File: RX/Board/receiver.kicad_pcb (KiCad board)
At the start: 2 copper layers, 31.8 x 76.2 mm, 16 parts, among them J1 CONN_SWITCH, J2 PROG_CONN, J3 RX_JMP, J4 TX_JMP, J5 AT_MODE_JUMP, J6 BATT_CONN, J7 GENERIC, U1 ARDUINO_PRO_MINI, U2 ITEAD_HC-05

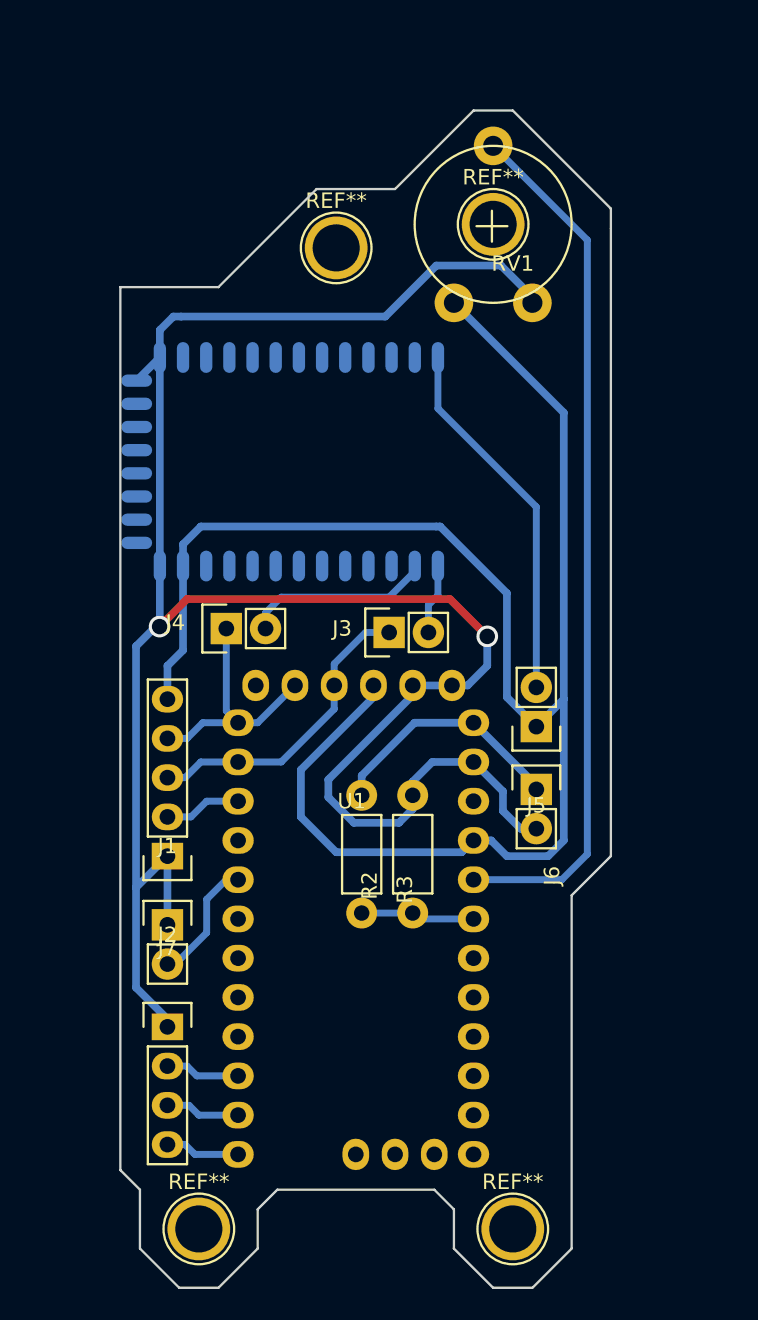
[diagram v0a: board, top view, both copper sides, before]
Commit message: Corrected bugs and added first prototype of receiver board
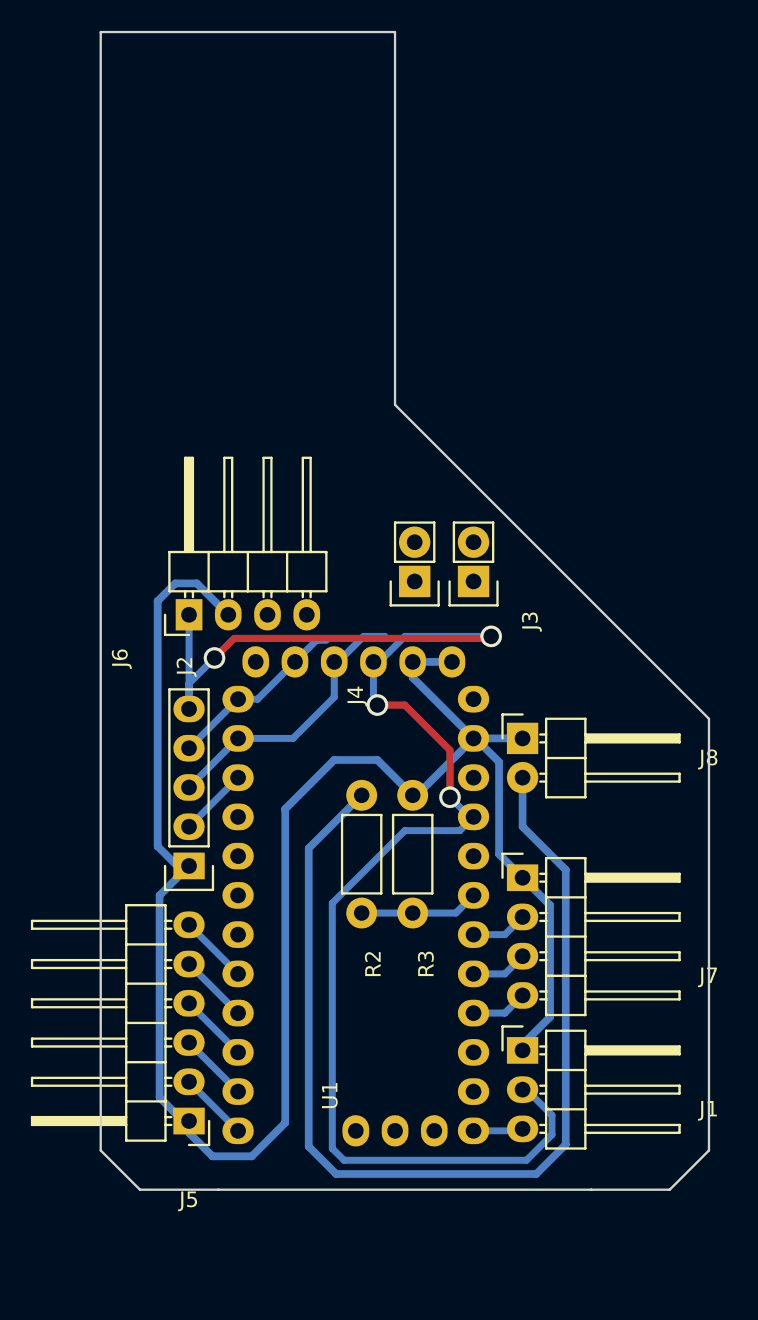
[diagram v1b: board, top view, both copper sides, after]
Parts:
- removed REF** (x4): 1pin, Connect:1pin
- removed RV1: POT, foots:Potenziometro_PIHER_10mm_diametro
- removed U2: ITEAD_HC-05, foots:HC-05
- added J8: BIG_BATTERY, Pin_Headers:Pin_Header_Angled_1x02, F.Cu at (169.5, 124.0)
- J1: value CONN_SWITCH -> ESC; footprint Pin_Headers:Pin_Header_Straight_1x02 -> Pin_Headers:Pin_Header_Angled_1x03
- J5: value AT_MODE_JUMP -> LIGHTS; footprint Pin_Headers:Pin_Header_Straight_1x02 -> Pin_Headers:Pin_Header_Angled_1x06
- J6: value BATT_CONN -> Bluetooth; footprint Pin_Headers:Pin_Header_Straight_1x02 -> Pin_Headers:Pin_Header_Angled_1x04
- J7: footprint Pin_Headers:Pin_Header_Straight_1x04 -> Pin_Headers:Pin_Header_Angled_1x04
- moved J5 34.0 mm to (148.0, 148.7)
- moved J6 25.2 mm to (148.0, 116.0), turned to 90 degrees
- moved J7 24.9 mm to (169.5, 133.0)
- moved J1 24.4 mm to (169.5, 144.1)
- moved J4 12.6 mm to (162.6, 113.8), turned to 180 degrees
- moved J3 6.38 mm to (166.4, 113.8), turned to 180 degrees
- moved J2 1.53 mm to (148.0, 132.2)
- moved U1 1.52 mm to (158.8, 118.9)
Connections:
- J1 pad 2: SWITCH_PRESENZA -> +5V
- J2 pad 5: +3V3 -> +5V
- J5 pad 1: +3V3 -> GNDREF
- J5 pad 2: AT_MODE -> LIGHT_1
- J6 pad 1: +BATT -> +5V
- U1 pad 10: G3 -> LIGHT_3
- U1 pad 11: G2 -> LIGHT_2
- U1 pad 12: G1 -> LIGHT_1
- U1 pad 16: (no net) -> ESC_SIG
- U1 pad 19: (no net) -> G1
- U1 pad 20: (no net) -> G2
- U1 pad 21: (no net) -> G3
- U1 pad 23: ACCEL_POT -> (no net)
- U1 pad 24: +3V3 -> +5V
- U1 pad 27: +BATT -> (no net)
- U1 pad 30: +3V3 -> +5V
- U1 pad 5: SWITCH_PRESENZA -> (no net)
- U1 pad 8: (no net) -> LIGHT_5
- U1 pad 9: (no net) -> LIGHT_4
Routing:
- net +3V3: track 112.9 -> 0.00 mm
- net +5V: track 0.00 -> 97.2 mm, vias 0 -> 4
- net ACCEL_POT: track 56.4 -> 0.00 mm
- net +BATT: track 15.9 -> 67.2 mm
- net AT_MODE: track 24.0 -> 0.00 mm
- net GNDREF: track 142.3 -> 122.8 mm, vias 2 -> 0
- net RX_BT: track 12.1 -> 0.00 mm
- net SWITCH_PRESENZA: track 8.10 -> 0.00 mm
- net TX_BT: track 4.55 -> 0.00 mm
- net LIGHT_5: track 0.00 -> 4.49 mm
- net LIGHT_4: track 0.00 -> 4.49 mm
- net LIGHT_2: track 0.00 -> 4.49 mm
- net LIGHT_1: track 0.00 -> 4.49 mm
- net LIGHT_3: track 0.00 -> 4.49 mm
- net TX_ARD: track 16.1 -> 11.8 mm
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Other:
- board size 31.8 x 76.2 mm -> 39.4 x 74.9 mm

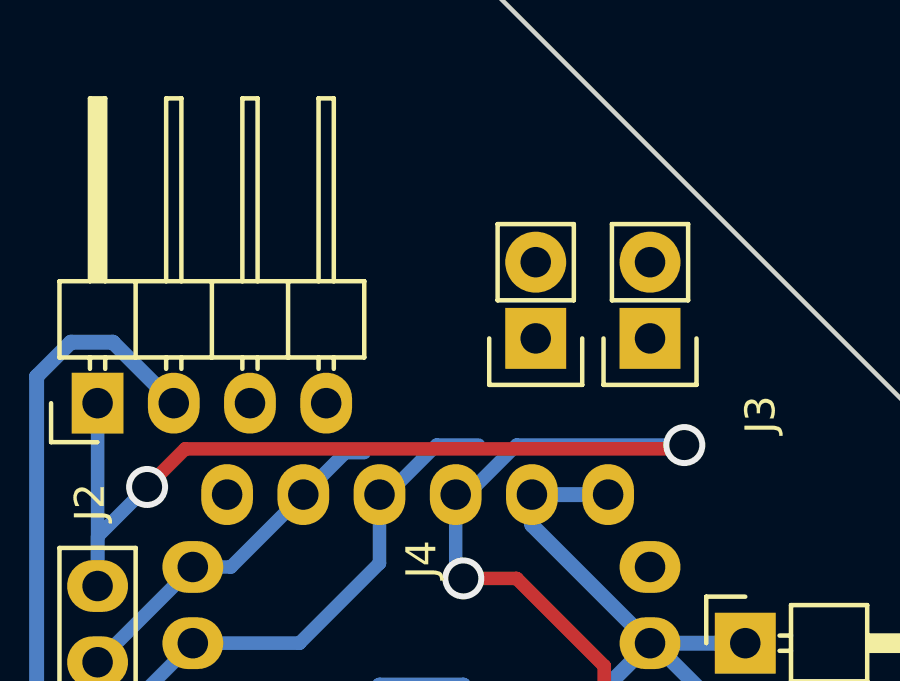
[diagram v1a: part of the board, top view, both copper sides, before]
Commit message: First working version of the receiver board
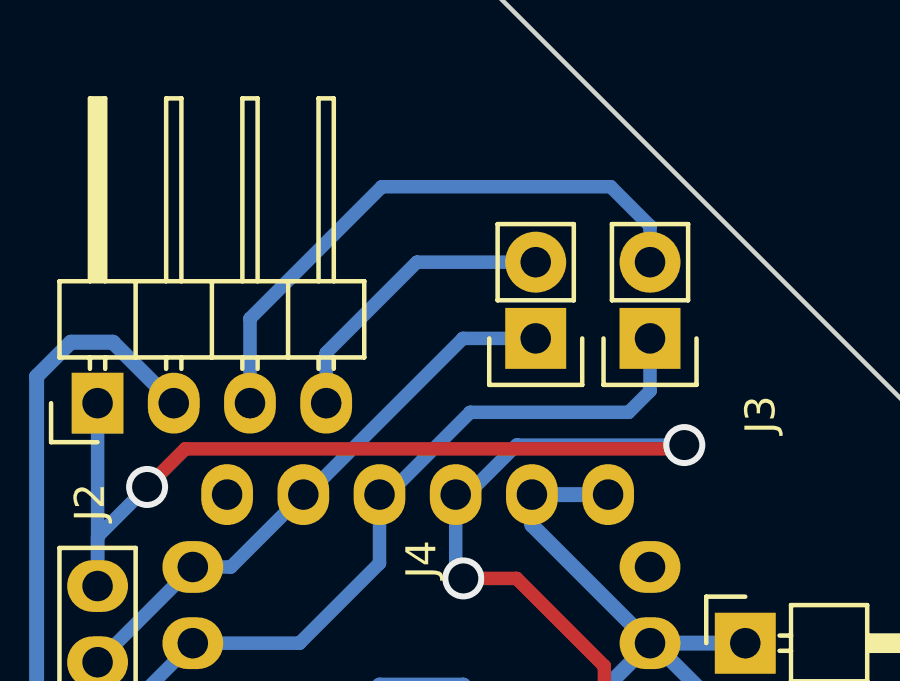
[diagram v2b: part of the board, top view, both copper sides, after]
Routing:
- net TX_BT: track 0.00 -> 19.7 mm
- net RX_BT: track 0.00 -> 9.91 mm
- net RX_ARD: track 18.1 -> 26.3 mm
- net TX_ARD: track 11.8 -> 19.1 mm
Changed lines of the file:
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@@
   (general
     (links 34)
-    (no_connects 4)
+    (no_connects 0)
     (area 137.079999 78.156999 189.675477 154.892)
     (thickness 1.6)
     (drawings 14)
-    (tracks 99)
+    (tracks 110)
     (zones 0)
     (modules 11)
@@
     (visible_elements FFFFFF7F)
     (pcbplotparams
-      (layerselection 0x01000_00000000)
+      (layerselection 0x00000_80000000)
       (usegerberextensions false)
       (excludeedgelayer true)
@@
   (segment (start 146.05 147.193) (end 146.05 134.112) (width 0.5) (layer B.Cu) (net 1))
   (segment (start 146.05 134.112) (end 147.955 132.207) (width 0.5) (layer B.Cu) (net 1) (status 20))
-  (segment (start 154.813 118.999) (end 156.21 117.602) (width 0.45) (layer B.Cu) (net 2) (status 10))
-  (segment (start 156.21 117.602) (end 156.845 117.602) (width 0.45) (layer B.Cu) (net 2))
+  (segment (start 154.813 118.999) (end 154.9273 118.999) (width 0.45) (layer B.Cu) (net 2) (status C00000))
+  (segment (start 154.9273 118.999) (end 160.1343 113.792) (width 0.45) (layer B.Cu) (net 2) (status 400000))
+  (segment (start 160.1343 113.792) (end 162.56 113.792) (width 0.45) (layer B.Cu) (net 2) (status 800000))
   (segment (start 151.13 121.412) (end 152.4 121.412) (width 0.45) (layer B.Cu) (net 2) (status 10))
   (segment (start 152.4 121.412) (end 154.813 118.999) (width 0.45) (layer B.Cu) (net 2) (status 20))
   (segment (start 147.955 124.587) (end 151.13 121.412) (width 0.45) (layer B.Cu) (net 2) (status 30))
-  (segment (start 157.353 118.999) (end 157.607 118.999) (width 0.45) (layer B.Cu) (net 3) (status 30))
-  (segment (start 157.607 118.999) (end 159.258 117.348) (width 0.45) (layer B.Cu) (net 3) (status 10))
-  (segment (start 159.258 117.348) (end 160.655 117.348) (width 0.45) (layer B.Cu) (net 3))
+  (segment (start 157.353 118.999) (end 157.6324 118.999) (width 0.45) (layer B.Cu) (net 3) (status C00000))
+  (segment (start 157.6324 118.999) (end 160.3756 116.2558) (width 0.45) (layer B.Cu) (net 3) (status 400000))
+  (segment (start 166.37 115.5446) (end 166.37 113.792) (width 0.45) (layer B.Cu) (net 3) (status 800000))
+  (segment (start 165.6588 116.2558) (end 166.37 115.5446) (width 0.45) (layer B.Cu) (net 3))
+  (segment (start 160.3756 116.2558) (end 165.6588 116.2558) (width 0.45) (layer B.Cu) (net 3))
   (segment (start 157.353 118.999) (end 157.353 121.285) (width 0.45) (layer B.Cu) (net 3) (status 10))
   (segment (start 154.686 123.952) (end 157.353 121.285) (width 0.45) (layer B.Cu) (net 3))
@@
   (segment (start 159.131 135.255) (end 162.433 135.255) (width 0.45) (layer B.Cu) (net 5) (status 30))
   (segment (start 147.955 129.667) (end 151.13 126.492) (width 0.45) (layer B.Cu) (net 6) (status 30))
+  (segment (start 166.37 111.252) (end 166.37 110.0455) (width 0.45) (layer B.Cu) (net 7) (status 400000))
+  (segment (start 153.035 113.1316) (end 153.035 115.951) (width 0.45) (layer B.Cu) (net 7) (status 800000))
+  (segment (start 157.4292 108.7374) (end 153.035 113.1316) (width 0.45) (layer B.Cu) (net 7))
+  (segment (start 165.0619 108.7374) (end 157.4292 108.7374) (width 0.45) (layer B.Cu) (net 7))
+  (segment (start 166.37 110.0455) (end 165.0619 108.7374) (width 0.45) (layer B.Cu) (net 7))
+  (segment (start 162.56 111.252) (end 158.5976 111.252) (width 0.45) (layer B.Cu) (net 8) (status 400000))
+  (segment (start 155.575 114.2746) (end 155.575 115.951) (width 0.45) (layer B.Cu) (net 8) (status 800000))
+  (segment (start 158.5976 111.252) (end 155.575 114.2746) (width 0.45) (layer B.Cu) (net 8))
   (segment (start 166.37 141.732) (end 168.402 141.732) (width 0.45) (layer B.Cu) (net 9) (status 10))
   (segment (start 168.402 141.732) (end 169.545 140.589) (width 0.45) (layer B.Cu) (net 9) (status 20))
